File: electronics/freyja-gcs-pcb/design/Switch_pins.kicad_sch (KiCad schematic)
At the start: 82 parts, among them J10 XT60PB-M.G.Y, J11 XT60PB-F.G.Y, Q10 NPN, Q11 NPN, Q12 NPN, Q13 NPN, Q14 NPN, Q15 NPN, Q16 NPN, Q17 NPN, Q18 NPN, Q19 NPN, Q20 NPN, Q21 NPN, Q22 NPN, Q23 NPN, Q9 NPN, SW10 PB22E09071, SW11 ST-0-102-A01-T000-LF+PJ, SW12 ST-0-102-A01-T000-LF+PJ, SW13 ST-0-102-A01-T000-LF+PJ, SW14 ST-0-102-A01-T000-LF+PJ, SW4 PB22E09071, SW5 ST-0-102-A01-T000-LF+PJ, SW6 ST-0-102-A01-T000-LF+PJ, SW7 PB22E09071, SW8 ST-0-102-A01-T000-LF+PJ, SW9 ST-0-102-A01-T000-LF+PJ

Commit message: footprint and lcsc part for all components
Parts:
- R39, R40, R45, R46, R51, R52, R56, R57, R61, R63, R66: footprint (none) -> Resistor_SMD:R_0603_1608Metric; LCSC Part (none) -> C23186
- R41, R42, R43, R44, R47, R48, R49, R50, R53, R54, R55, R58, R59: footprint EasyEDA:R0603 -> Resistor_SMD:R_0603_1608Metric
- R60, R62, R64, R65: footprint (none) -> Resistor_SMD:R_0603_1608Metric; LCSC Part (none) -> C22962
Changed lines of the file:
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@@
 			)
 		)
-		(property "Footprint" "EasyEDA:R0603"
+		(property "Footprint" "Resistor_SMD:R_0603_1608Metric"
 			(at 132.842 95.25 90)
 			(effects
@@
 			)
 		)
-		(property "Footprint" ""
+		(property "Footprint" "Resistor_SMD:R_0603_1608Metric"
 			(at 235.458 26.67 90)
 			(effects
@@
 			)
 		)
+		(property "LCSC Part" "C22962"
+			(at 233.68 26.67 0)
+			(effects
+				(font
+					(size 1.27 1.27)
+				)
+				(hide yes)
+			)
+		)
 		(pin "2"
 		)
@@
 			)
 		)
-		(property "Footprint" "EasyEDA:R0603"
+		(property "Footprint" "Resistor_SMD:R_0603_1608Metric"
 			(at 44.45 152.908 90)
 			(effects
@@
 			)
 		)
-		(property "Footprint" "EasyEDA:R0603"
+		(property "Footprint" "Resistor_SMD:R_0603_1608Metric"
 			(at 132.842 48.26 90)
 			(effects
@@
 			)
 		)
-		(property "Footprint" "EasyEDA:R0603"
+		(property "Footprint" "Resistor_SMD:R_0603_1608Metric"
 			(at 140.462 172.72 90)
 			(effects
@@
 			)
 		)
-		(property "Footprint" ""
+		(property "Footprint" "Resistor_SMD:R_0603_1608Metric"
 			(at 215.138 26.67 90)
 			(effects
@@
 			)
 		)
+		(property "LCSC Part" "C22962"
+			(at 213.36 26.67 0)
+			(effects
+				(font
+					(size 1.27 1.27)
+				)
+				(hide yes)
+			)
+		)
 		(pin "2"
 		)
@@
 			)
 		)
-		(property "Footprint" ""
+		(property "Footprint" "Resistor_SMD:R_0603_1608Metric"
 			(at 255.778 26.67 90)
 			(effects
@@
 			)
 		)
+		(property "LCSC Part" "C22962"
+			(at 254 26.67 0)
+			(effects
+				(font
+					(size 1.27 1.27)
+				)
+				(hide yes)
+			)
+		)
 		(pin "2"
 		)
@@
 			)
 		)
-		(property "Footprint" ""
+		(property "Footprint" "Resistor_SMD:R_0603_1608Metric"
 			(at 164.338 25.4 90)
 			(effects
@@
 			)
 		)
+		(property "LCSC Part" "C23186"
+			(at 162.56 25.4 0)
+			(effects
+				(font
+					(size 1.27 1.27)
+				)
+				(hide yes)
+			)
+		)
 		(pin "2"
 		)
@@
 			)
 		)
-		(property "Footprint" ""
+		(property "Footprint" "Resistor_SMD:R_0603_1608Metric"
 			(at 34.798 25.4 90)
 			(effects
@@
 			)
 		)
+		(property "LCSC Part" "C23186"
+			(at 33.02 25.4 0)
+			(effects
+				(font
+					(size 1.27 1.27)
+				)
+				(hide yes)
+			)
+		)
 		(pin "2"
 		)
@@
 			)
 		)
-		(property "Footprint" ""
+		(property "Footprint" "Resistor_SMD:R_0603_1608Metric"
 			(at 34.798 72.39 90)
 			(effects
@@
 			)
 		)
+		(property "LCSC Part" "C23186"
+			(at 33.02 72.39 0)
+			(effects
+				(font
+					(size 1.27 1.27)
+				)
+				(hide yes)
+			)
+		)
 		(pin "2"
 		)
@@
 			)
 		)
-		(property "Footprint" "EasyEDA:R0603"
+		(property "Footprint" "Resistor_SMD:R_0603_1608Metric"
 			(at 51.562 172.72 90)
 			(effects
@@
 			)
 		)
-		(property "Footprint" ""
+		(property "Footprint" "Resistor_SMD:R_0603_1608Metric"
 			(at 215.138 74.93 90)
 			(effects
@@
 			)
 		)
+		(property "LCSC Part" "C23186"
+			(at 213.36 74.93 0)
+			(effects
+				(font
+					(size 1.27 1.27)
+				)
+				(hide yes)
+			)
+		)
 		(pin "2"
 		)
@@
 			)
 		)
-		(property "Footprint" "EasyEDA:R0603"
+		(property "Footprint" "Resistor_SMD:R_0603_1608Metric"
 			(at 46.482 48.26 90)
 			(effects
@@
 			)
 		)
-		(property "Footprint" "EasyEDA:R0603"
+		(property "Footprint" "Resistor_SMD:R_0603_1608Metric"
 			(at 176.022 95.25 90)
 			(effects
@@
 			)
 		)
-		(property "Footprint" ""
+		(property "Footprint" "Resistor_SMD:R_0603_1608Metric"
 			(at 235.458 74.93 90)
 			(effects
@@
 			)
 		)
+		(property "LCSC Part" "C23186"
+			(at 233.68 74.93 0)
+			(effects
+				(font
+					(size 1.27 1.27)
+				)
+				(hide yes)
+			)
+		)
 		(pin "2"
 		)
@@
 			)
 		)
-		(property "Footprint" ""
+		(property "Footprint" "Resistor_SMD:R_0603_1608Metric"
 			(at 121.158 72.39 90)
 			(effects
@@
 			)
 		)
+		(property "LCSC Part" "C23186"
+			(at 119.38 72.39 0)
+			(effects
+				(font
+					(size 1.27 1.27)
+				)
+				(hide yes)
+			)
+		)
 		(pin "2"
 		)
@@
 			)
 		)
-		(property "Footprint" "EasyEDA:R0603"
+		(property "Footprint" "Resistor_SMD:R_0603_1608Metric"
 			(at 89.662 48.26 90)
 			(effects
@@
 			)
 		)
-		(property "Footprint" "EasyEDA:R0603"
+		(property "Footprint" "Resistor_SMD:R_0603_1608Metric"
 			(at 96.012 172.72 90)
 			(effects
@@
 			)
 		)
-		(property "Footprint" "EasyEDA:R0603"
+		(property "Footprint" "Resistor_SMD:R_0603_1608Metric"
 			(at 46.482 95.25 90)
 			(effects
@@
 			)
 		)
-		(property "Footprint" ""
+		(property "Footprint" "Resistor_SMD:R_0603_1608Metric"
 			(at 77.978 25.4 90)
 			(effects
@@
 			)
 		)
+		(property "LCSC Part" "C23186"
+			(at 76.2 25.4 0)
+			(effects
+				(font
+					(size 1.27 1.27)
+				)
+				(hide yes)
+			)
+		)
 		(pin "2"
 		)
@@
 			)
 		)
-		(property "Footprint" ""
+		(property "Footprint" "Resistor_SMD:R_0603_1608Metric"
 			(at 164.338 72.39 90)
 			(effects
@@
 			)
 		)
+		(property "LCSC Part" "C23186"
+			(at 162.56 72.39 0)
+			(effects
+				(font
+					(size 1.27 1.27)
+				)
+				(hide yes)
+			)
+		)
 		(pin "2"
 		)
@@
 			)
 		)
-		(property "Footprint" ""
+		(property "Footprint" "Resistor_SMD:R_0603_1608Metric"
 			(at 255.778 74.93 90)
 			(effects
@@
 			)
 		)
+		(property "LCSC Part" "C22962"
+			(at 254 74.93 0)
+			(effects
+				(font
+					(size 1.27 1.27)
+				)
+				(hide yes)
+			)
+		)
 		(pin "2"
 		)
@@
 			)
 		)
-		(property "Footprint" "EasyEDA:R0603"
+		(property "Footprint" "Resistor_SMD:R_0603_1608Metric"
 			(at 89.662 95.25 90)
 			(effects
@@
 			)
 		)
-		(property "Footprint" ""
+		(property "Footprint" "Resistor_SMD:R_0603_1608Metric"
 			(at 276.098 26.67 90)
 			(effects
@@
 			)
 		)
+		(property "LCSC Part" "C23186"
+			(at 274.32 26.67 0)
+			(effects
+				(font
+					(size 1.27 1.27)
+				)
+				(hide yes)
+			)
+		)
 		(pin "2"
 		)
@@
 			)
 		)
-		(property "Footprint" ""
+		(property "Footprint" "Resistor_SMD:R_0603_1608Metric"
 			(at 77.978 72.39 90)
 			(effects
@@
 			)
 		)
+		(property "LCSC Part" "C23186"
+			(at 76.2 72.39 0)
+			(effects
+				(font
+					(size 1.27 1.27)
+				)
+				(hide yes)
+			)
+		)
 		(pin "2"
 		)
@@
 			)
 		)
-		(property "Footprint" "EasyEDA:R0603"
+		(property "Footprint" "Resistor_SMD:R_0603_1608Metric"
 			(at 176.022 48.26 90)
 			(effects
@@
 			)
 		)
-		(property "Footprint" "EasyEDA:R0603"
+		(property "Footprint" "Resistor_SMD:R_0603_1608Metric"
 			(at 88.9 152.908 90)
 			(effects
@@
 			)
 		)
-		(property "Footprint" ""
+		(property "Footprint" "Resistor_SMD:R_0603_1608Metric"
 			(at 121.158 25.4 90)
 			(effects
@@
 			(at 119.38 25.4 0)
 			(effects
+				(font
+					(size 1.27 1.27)
+				)
+				(hide yes)
+			)
+		)
+		(property "LCSC Part" "C23186"
+			(at 119.38 25.4 0)
+			(effects

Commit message: 3d model improvement
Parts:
- J11: footprint EasyEDA:CONN-TH_XT60PB-M -> EasyEDA:CONN-TH_XT60PB-F.G.Y
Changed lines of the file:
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@@
 			)
 		)
-		(property "Footprint" "EasyEDA:CONN-TH_XT60PB-M"
+		(property "Footprint" "EasyEDA:CONN-TH_XT60PB-F.G.Y"
 			(at 101.6 139.7 0)
 			(effects

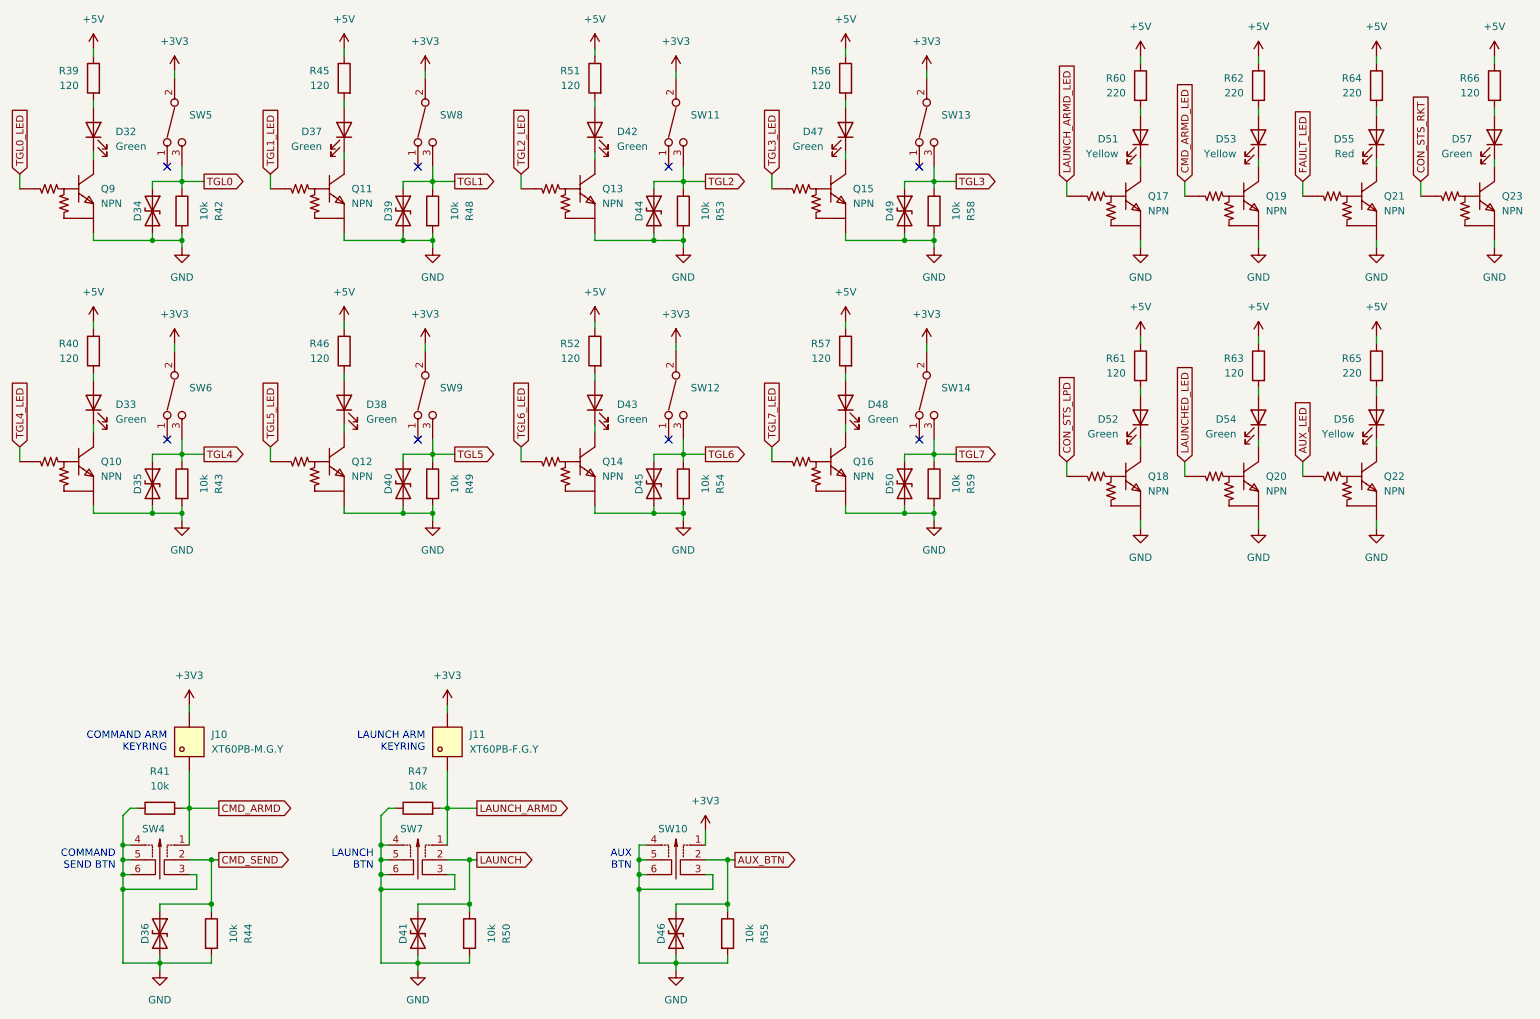
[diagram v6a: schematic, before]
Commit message: locked position of components
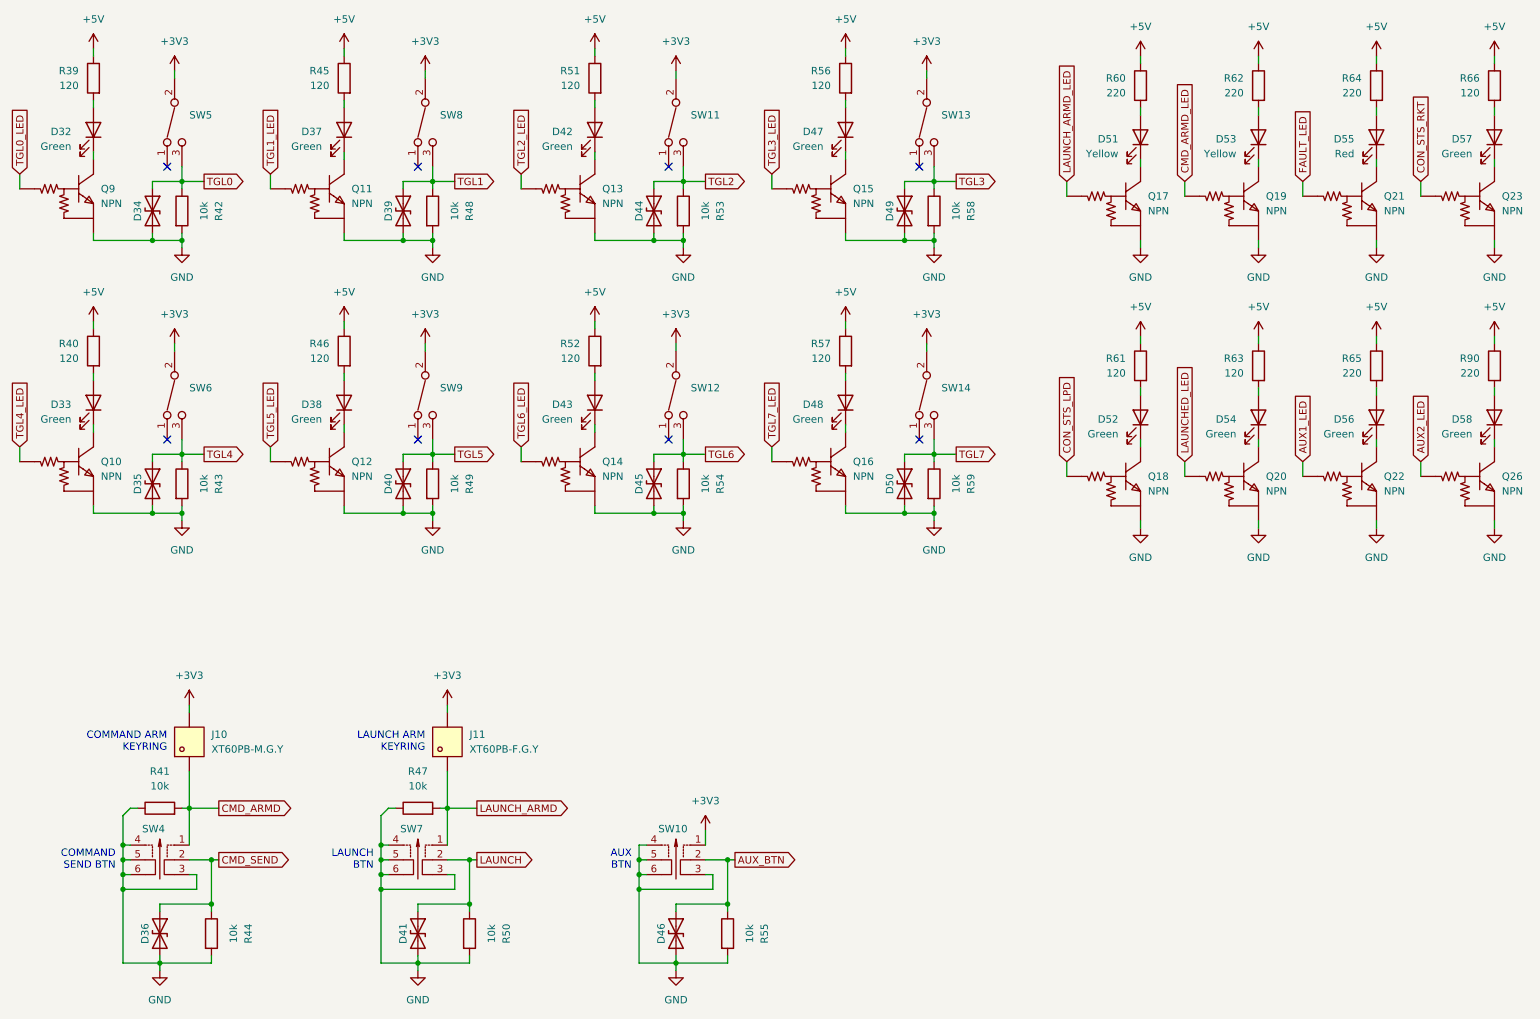
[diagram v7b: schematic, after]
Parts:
- added D58: Green, EasyEDA:LED-TH_BD5.9-P2.54-RD_GREEN, symbol Device:LED
- added Q26: NPN, EasyEDA:SOT-416_L1.6-W0.8-P1.00-LS1.6-BR, symbol EasyEDA:DTC043ZEBTL
- added R90: 220, Resistor_SMD:R_0603_1608Metric, symbol Device:R
- D56: value Yellow -> Green; LCSC Part C2895494 -> C2895548
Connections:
- net +5V: now also R90.1
- net GND: now also Q26.2 (E)
- net AUX_LED renamed AUX1_LED
- new net: D58.1 (K), Q26.3 (C)
- new net: D58.2 (A), R90.2
- new net AUX2_LED: Q26.1 (B)
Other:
- moved on the sheet: D32, D33, D38, D42, D43, D48

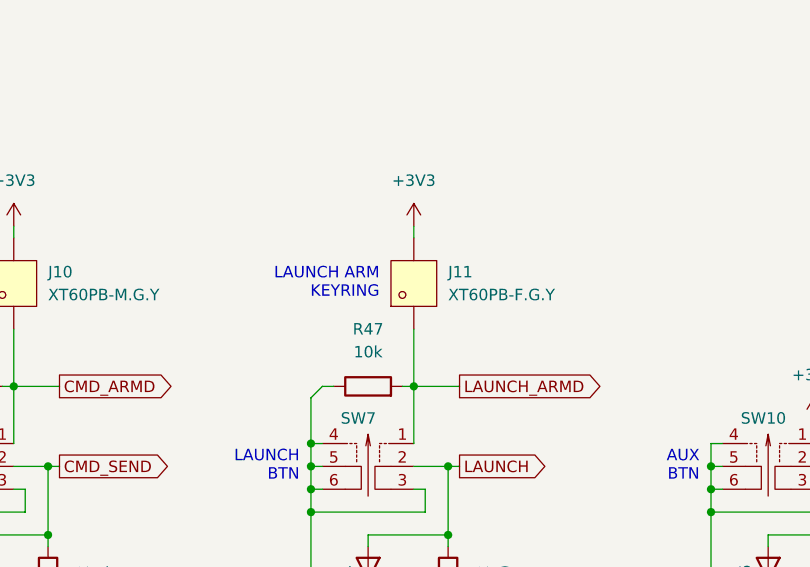
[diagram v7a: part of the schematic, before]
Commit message: fix footprints
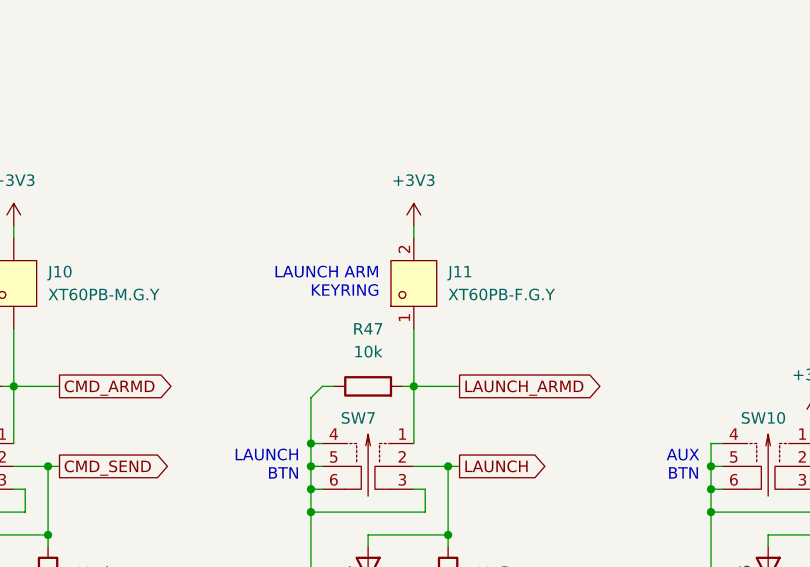
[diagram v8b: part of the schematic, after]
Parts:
- J11: symbol EasyEDA:XT60PB-M.G.Y -> EasyEDA:XT60PB-F.G.Y; LCSC Part C19268037 -> C19268038
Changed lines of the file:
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@@
 	)
 	(symbol
-		(lib_name "XT60PB-M.G.Y_1")
-		(lib_id "EasyEDA:XT60PB-M.G.Y")
+		(lib_id "EasyEDA:XT60PB-F.G.Y")
 		(at 93.98 139.7 90)
 		(unit 1)
@@
 		)
 		(property "Footprint" "EasyEDA:CONN-TH_XT60PB-F.G.Y"
-			(at 101.6 139.7 0)
+			(at 102.87 139.7 0)
 			(effects
 				(font
@@
 			)
 		)
-		(property "LCSC Part" "C19268037"
-			(at 104.14 139.7 0)
+		(property "LCSC Part" "C19268038"
+			(at 105.41 139.7 0)
 			(effects
 				(font
